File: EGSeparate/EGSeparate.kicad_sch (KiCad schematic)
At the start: 20 parts, among them IC1 PIC16F15325-I_P, IC2 MCP6232-E_P, J1 ICSP, J2 D_Power, J4 Conn_01x04, J5 Conn_01x03, SW1 2MS1T1B4VS2QES

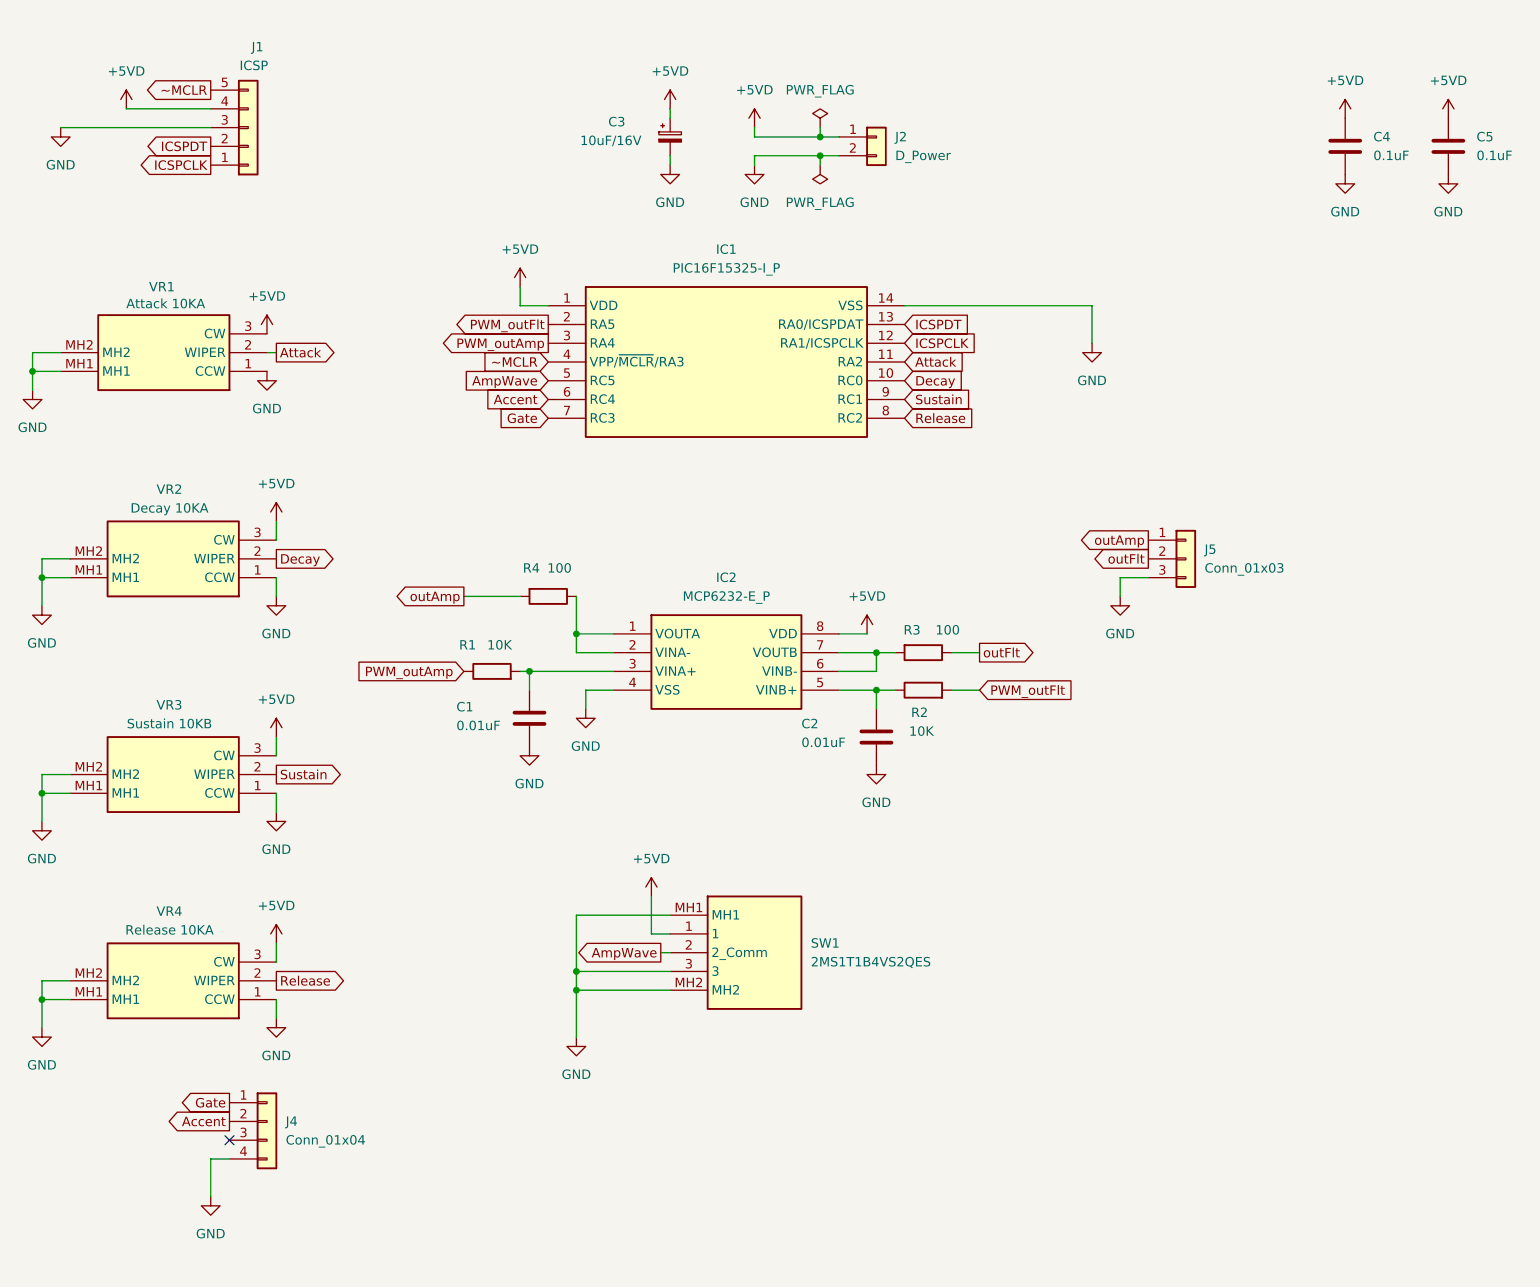
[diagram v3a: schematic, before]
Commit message: MC2
アクセントレベルを追加したEGACCを登録
回路全般部品配置済
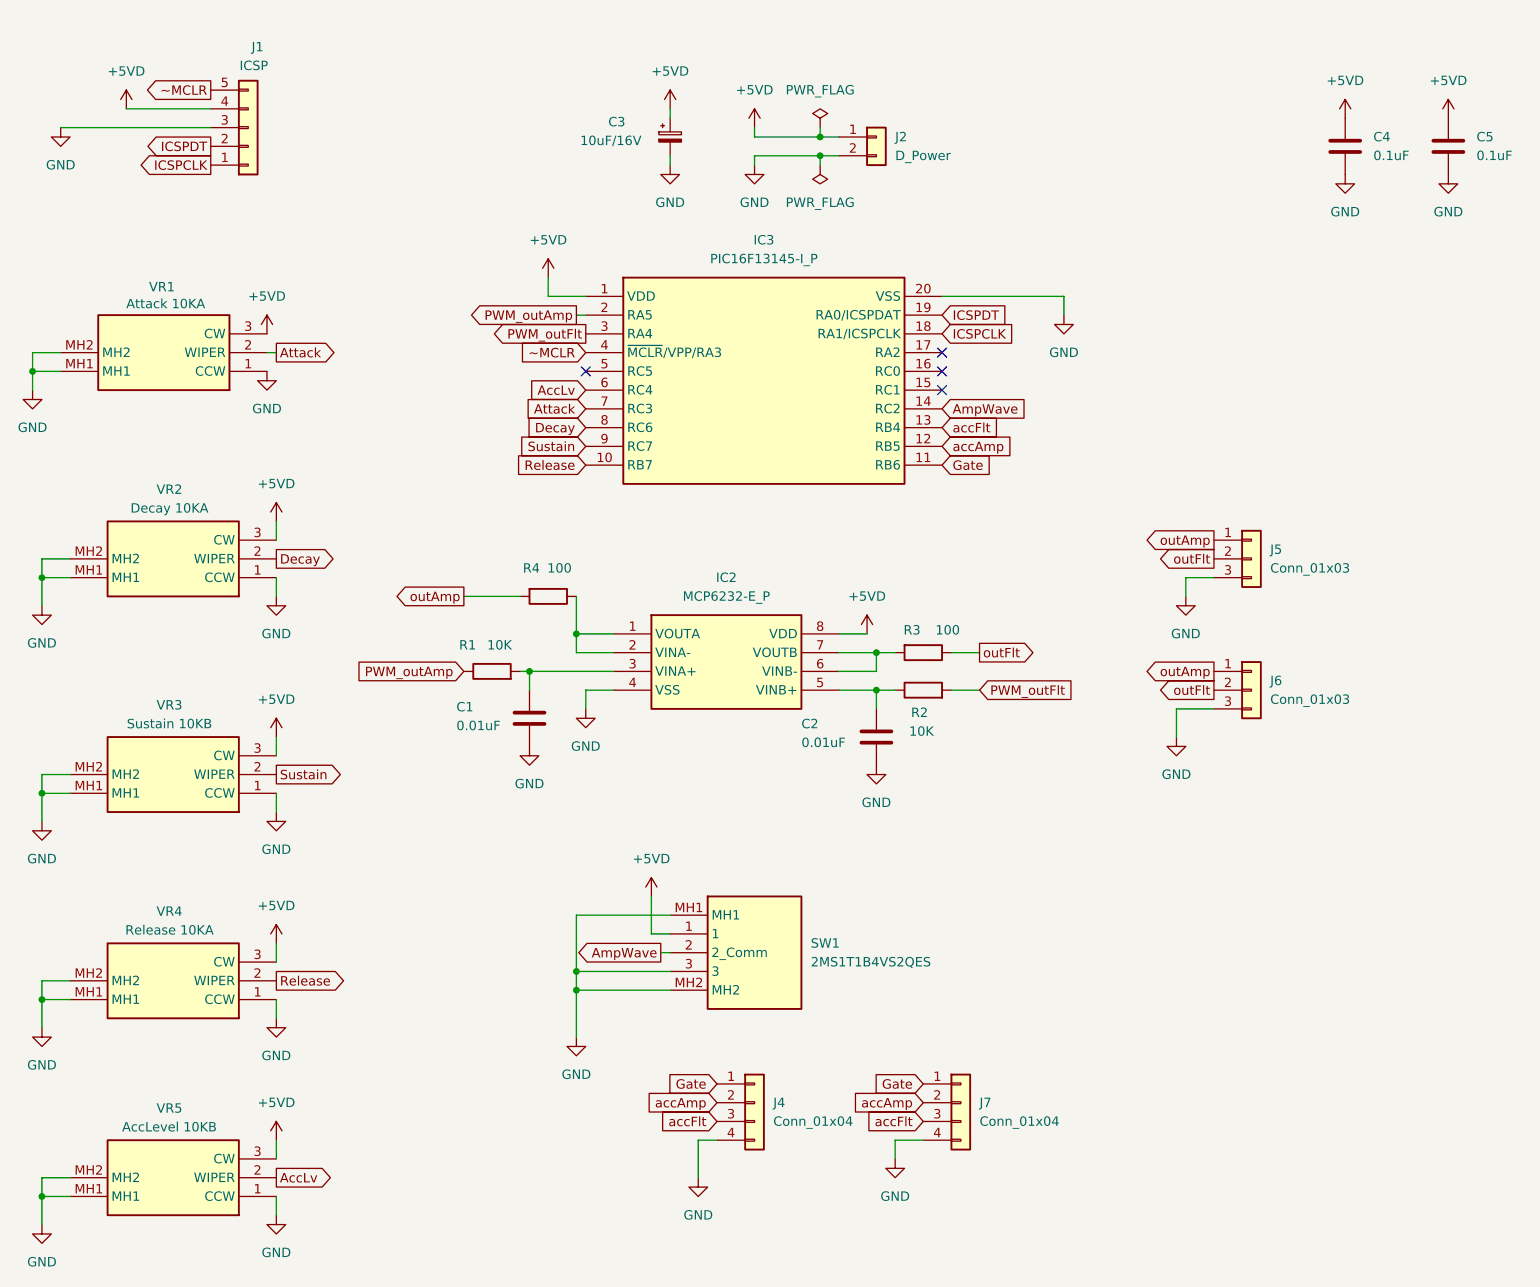
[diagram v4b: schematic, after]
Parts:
- removed IC1: PIC16F15325-I_P, DIP781W56P254L1918H533Q14N, symbol SamacSys_Parts:PIC16F15325-I_P
- added IC3: PIC16F13145-I_P, DIP794W56P254L2591H533Q20N, symbol SamacSys_Parts:PIC16F13145-I_P
- added J6: Conn_01x03, Connector_PinSocket_2.54mm:PinSocket_1x03_P2.54mm_Vertical, symbol Connector_Generic:Conn_01x03
- added J7: Conn_01x04, Connector_PinHeader_2.54mm:PinHeader_1x04_P2.54mm_Vertical, symbol Connector_Generic:Conn_01x04
- added VR5: AccLevel 10KB, SamacSys_Parts:RK09D117000B, symbol SamacSys_Parts:RK09D117000B
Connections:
- net +5VD: now also IC3.1 (VDD), VR5.3 (CW)
- net AmpWave: now also IC3.14 (RC2)
- net Attack: now also IC3.7 (RC3)
- net Decay: now also IC3.8 (RC6)
- net GND: now also IC3.20 (VSS), J6.3 (Pin_3), J7.4 (Pin_4), VR5.1 (CCW), VR5.MH1, VR5.MH2
- net Gate: now also IC3.11 (RB6), J7.1 (Pin_1)
- net ICSPCLK: now also IC3.18 (RA1/ICSPCLK)
- net ICSPDT: now also IC3.19 (RA0/ICSPDAT)
- net PWM_outAmp: now also IC3.2 (RA5)
- net PWM_outFlt: now also IC3.3 (RA4)
- net Release: now also IC3.10 (RB7)
- net Sustain: now also IC3.9 (RC7)
- net outAmp: now also J6.1 (Pin_1)
- net outFlt: now also J6.2 (Pin_2)
- net ~MCLR: now also IC3.4 (~{MCLR}/VPP/RA3)
- net accFlt: now reaches J4.3 (Pin_3)
- net accFlt: now also IC3.13 (RB4), J7.3 (Pin_3)
- net Accent renamed accAmp
- net accAmp: now also IC3.12 (RB5), J7.2 (Pin_2)
- new net AccLv: IC3.6 (RC4), VR5.2 (WIPER)
- no-connect marks 1 -> 4
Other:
- moved on the sheet: J4, J5

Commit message: EGSeparater
~MCLRのリセット回路を追加
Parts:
- added C6: 0.01uF, Capacitor_THT:C_Disc_D3.4mm_W2.1mm_P2.50mm, symbol Device:C
- added R5: 1K, Resistor_THT:R_Axial_DIN0204_L3.6mm_D1.6mm_P2.54mm_Vertical, symbol Device:R
- added R6: 100, Resistor_THT:R_Axial_DIN0204_L3.6mm_D1.6mm_P2.54mm_Vertical, symbol Device:R
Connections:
- net +5VD: now also R5.1
- net GND: now also C6.2
- net PWM_outAmp: now also IC3.15 (RC1); no longer IC3.2 (RA5)
- net ~MCLR: now also R6.1
- new net: C6.1, R5.2, R6.2
